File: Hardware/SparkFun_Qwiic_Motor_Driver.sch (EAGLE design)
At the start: 44 parts, among them J1 Power In, J2 Motor Connections, J3 Qwiic, J4 Qwiic, U1 DRV8835, U2 CY8C4245LQI-483

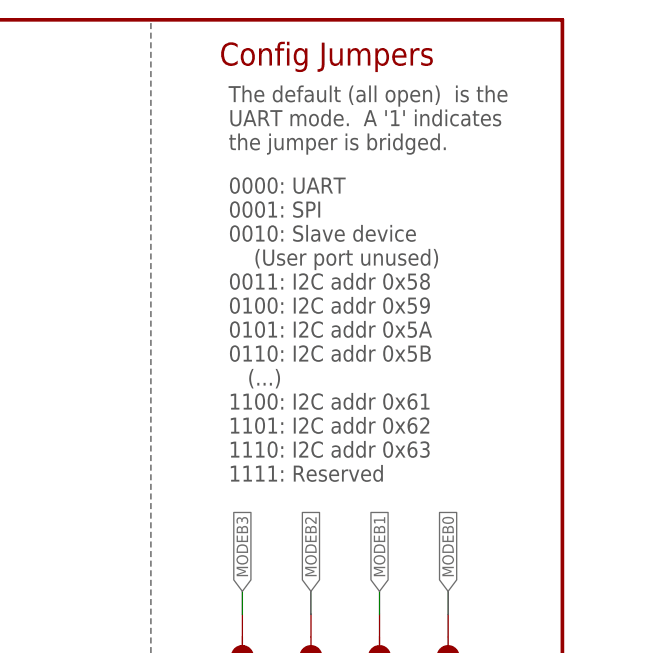
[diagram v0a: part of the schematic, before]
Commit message: Update SparkFun_Qwiic_Motor_Driver.sch
Updated the config jumpers section of the schematic of valid addresses
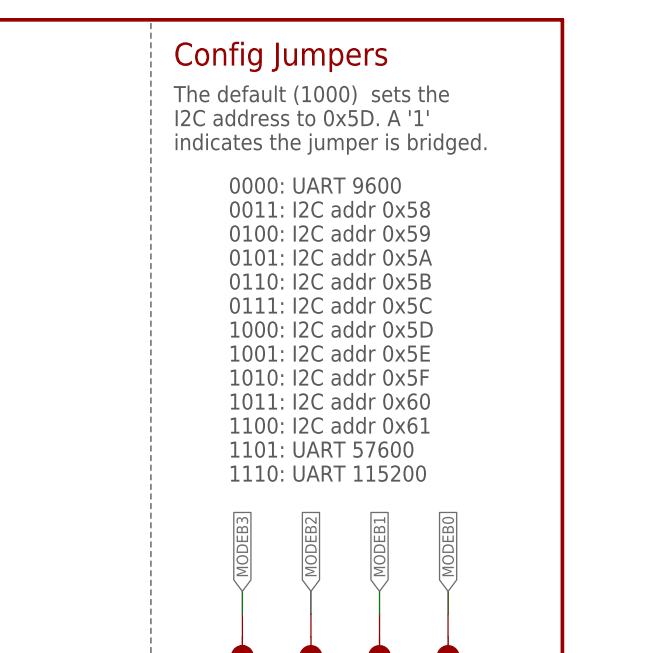
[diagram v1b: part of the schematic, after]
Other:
- note added: "0000: UART 9600 0011: I2C addr 0x58 0100: I2C addr 0x59 0101: I2C addr 0x5A 0110: I2C addr 0x5B 0111: I2C addr 0x5C 1000: I2C addr 0x5D 1001: I2C addr 0x5E 1010: I2C addr 0x5F 1011: I2C addr 0x60 1100: I2C addr 0x61 1101: UART 57600 1110: UART 115200"
- note added: "The default (1000) sets the I2C address to 0x5D. A '1' indicates the jumper is bridged."
- note removed: "0000: UART 0001: SPI 0010: Slave device (User port unused) 0011: I2C addr 0x58 0100: I2C addr 0x59 0101: I2C addr 0x5A 0110: I2C addr 0x5B (...) 1100: I2C addr 0x61 1101: I2C addr 0x62 1110: I2C addr 0x63 1111: Reserved"
- note removed: "The default (all open) is the UART mode. A '1' indicates the jumper is bridged."
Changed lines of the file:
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@@
 <?xml version="1.0" encoding="utf-8"?>
 <!DOCTYPE eagle SYSTEM "eagle.dtd">
-<eagle version="9.4.1">
+<eagle version="9.5.0">
 <drawing>
 <settings>
@@
 <plain>
 <text x="2.54" y="53.34" size="2.54" layer="94" font="vector" ratio="15">PSoC Power and Filtering</text>
-<text x="210.82" y="180.34" size="2.54" layer="94" font="vector" ratio="15">Config Jumpers</text>
+<text x="205.74" y="180.34" size="2.54" layer="94" font="vector" ratio="15">Config Jumpers</text>
 <text x="166.624" y="11.43" size="2.54" layer="94" font="vector">Alex Wende</text>
 <text x="2.54" y="93.98" size="2.54" layer="94" font="vector" ratio="15">PSoC I/O</text>
@@
 P3.3 swd_clk[0]
 </text>
-<text x="211.836" y="167.894" size="1.778" layer="97" font="vector" align="top-left">0000: UART
-0001: SPI
-0010: Slave device
-    (User port unused)
+<text x="211.836" y="167.894" size="1.778" layer="97" font="vector" align="top-left">0000: UART 9600
 0011: I2C addr 0x58
 0100: I2C addr 0x59
 0101: I2C addr 0x5A
 0110: I2C addr 0x5B
-   (...)
+0111: I2C addr 0x5C
+1000: I2C addr 0x5D
+1001: I2C addr 0x5E
+1010: I2C addr 0x5F
+1011: I2C addr 0x60
 1100: I2C addr 0x61
-1101: I2C addr 0x62
-1110: I2C addr 0x63
-1111: Reserved</text>
-<text x="211.836" y="178.054" size="1.778" layer="97" font="vector" align="top-left">The default (all open)  is the
-UART mode.  A '1' indicates
-the jumper is bridged.</text>
+1101: UART 57600
+1110: UART 115200</text>
+<text x="205.74" y="178.054" size="1.778" layer="97" font="vector" align="top-left">The default (1000)  sets the
+I2C address to 0x5D. A '1'
+indicates the jumper is bridged.</text>
 <text x="2.54" y="180.34" size="2.54" layer="94" font="vector" ratio="15">Connectors</text>
 <text x="66.04" y="180.34" size="2.54" layer="94" font="vector" ratio="15">Status LED</text>
